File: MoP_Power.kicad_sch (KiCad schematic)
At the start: 0 parts

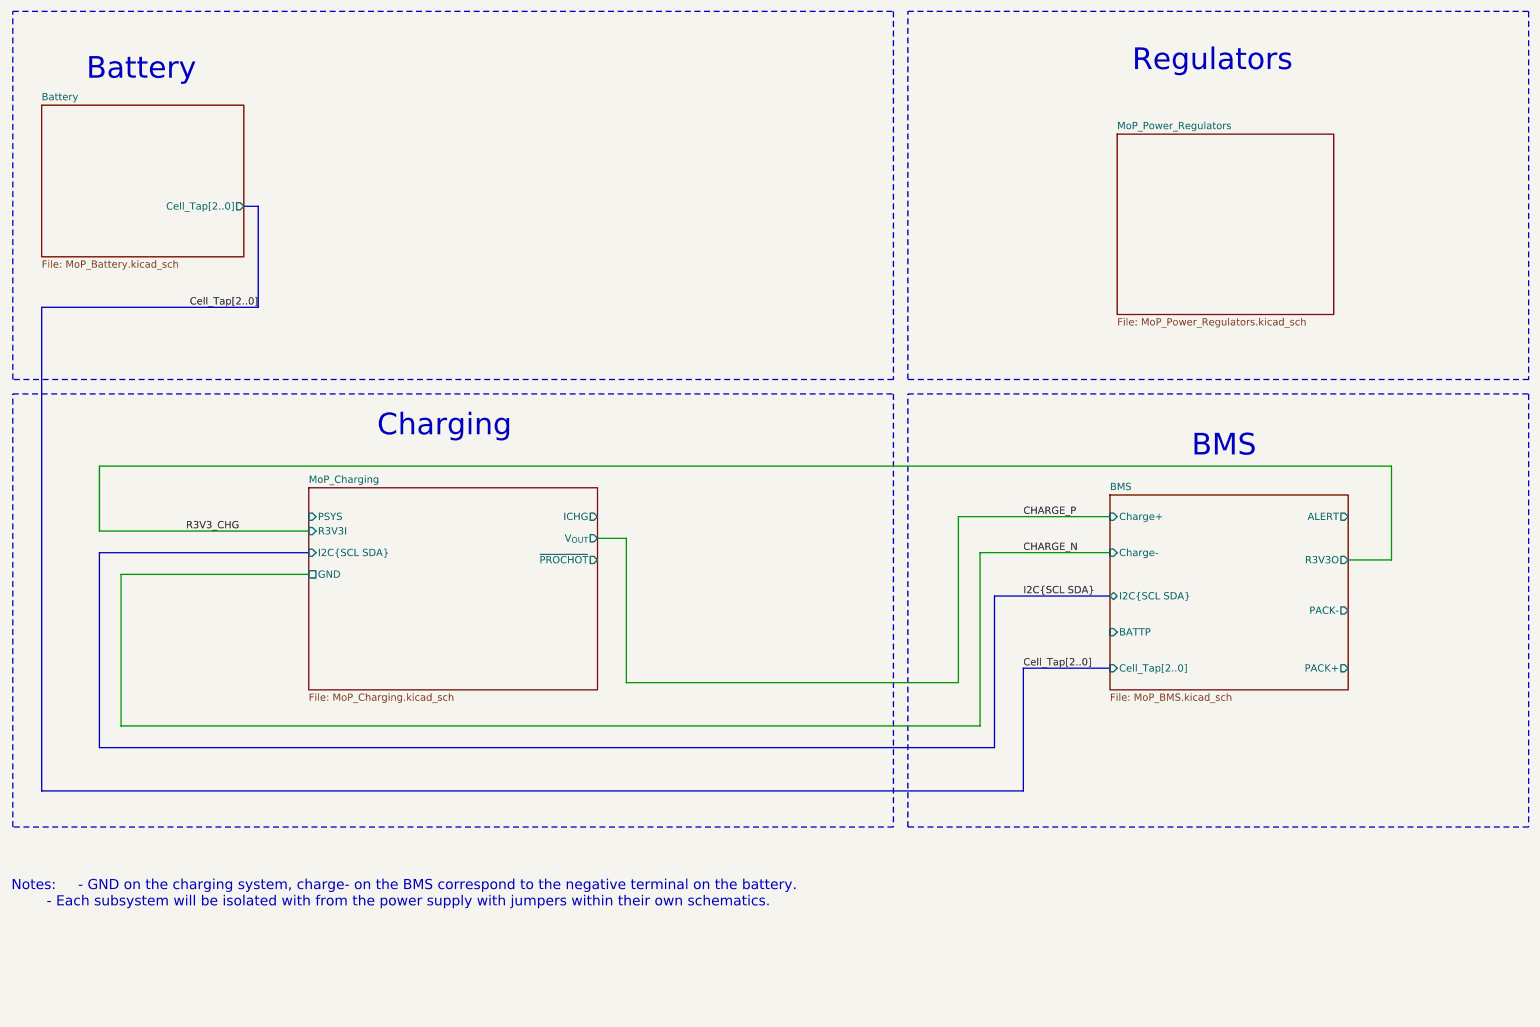
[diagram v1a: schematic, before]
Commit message: changed ref designators to be consistent accross sheets
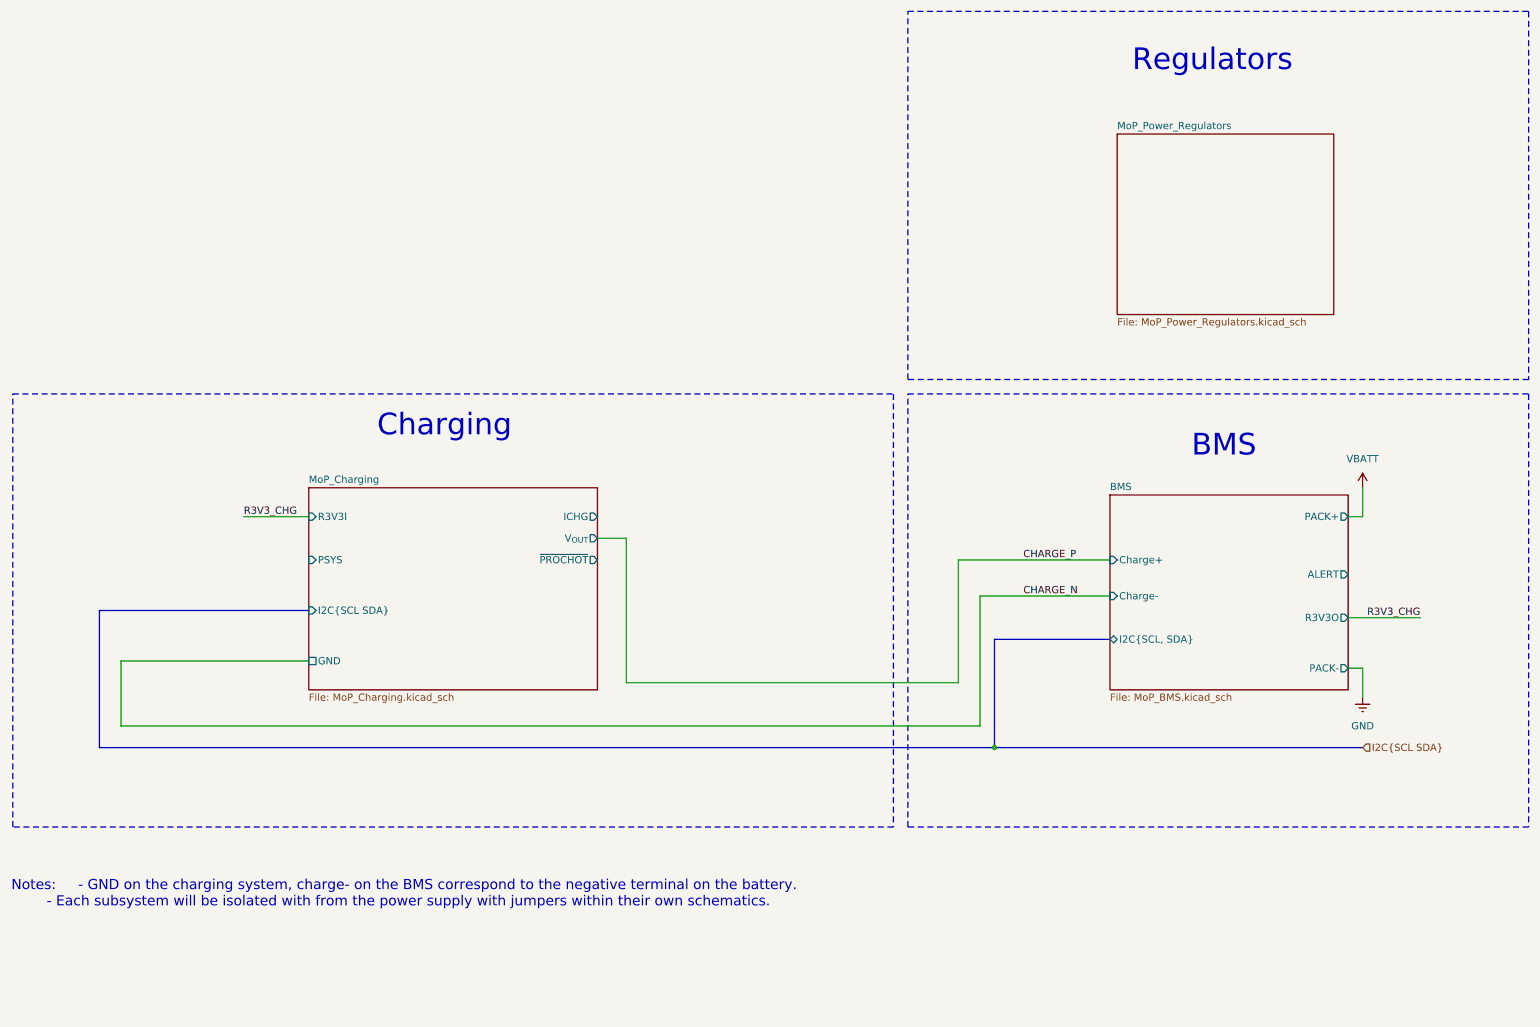
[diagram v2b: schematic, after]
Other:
- removed sheet Battery
- sheet BMS ports: added I2C{SCL, SDA}; removed BATTP, Cell_Tap[2..0], I2C{SCL SDA}
- note removed: "Battery"

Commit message: Finished schematics
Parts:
- added J201: Jumper, Connector_PinHeader_2.54mm:PinHeader_1x02_P2.54mm_Vertical, symbol Jumper:Jumper_2_Bridged
- added R1: R, Resistor_SMD:R_0805_2012Metric, symbol Device:R
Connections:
- net VBATT: now also J201.2 (B), R1.2
- new net BMS/PACK+: J201.1 (A), R1.1
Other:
- note added: "Notes: - GND system wide corresponds to the PACK- connecion to the BMS system. - VBATT does not mean the positive terminal of the battery. it corresponds to the voltage supplied by the BMS from the battery. - Each subsystem will be isolated from the power supply with jumpers within their own schematics. - There are no hierarchichal connectors shown for the power regulators sheet because the power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"
- note removed: "Notes: - GND on the charging system, charge- on the BMS correspond to the negative terminal on the battery. - Each subsystem will be isolated with from the power supply with jumpers within their own schematics."
